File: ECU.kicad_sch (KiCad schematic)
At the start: 6 parts

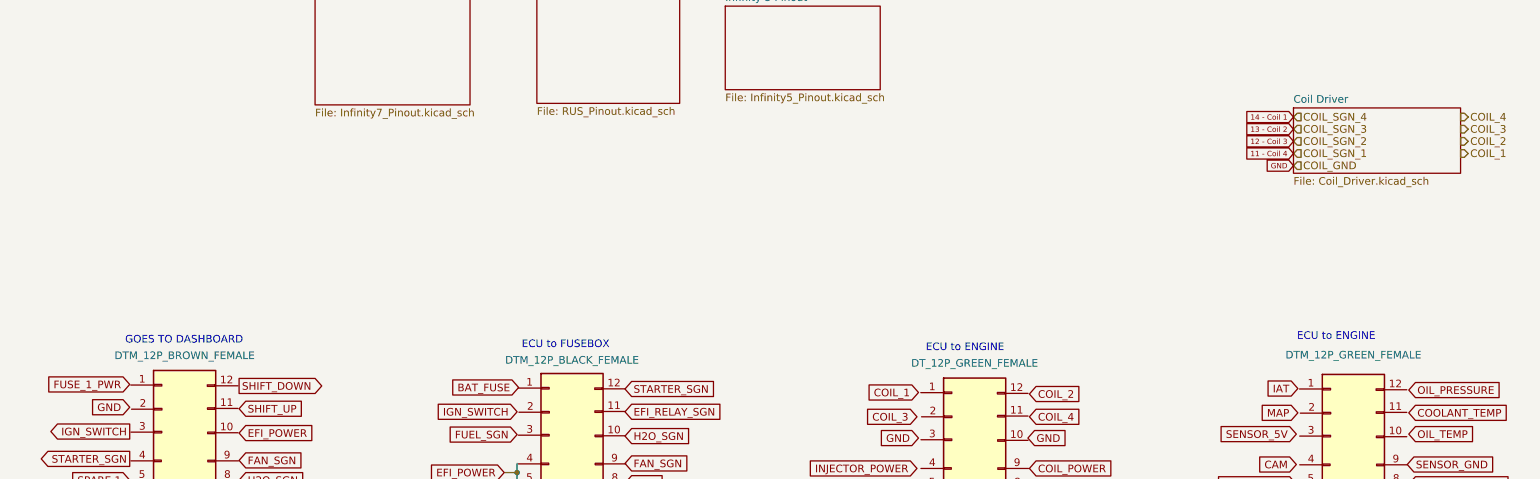
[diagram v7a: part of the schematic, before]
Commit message: Connector Numbers 1
Added Numbers to all of the connectors that were numbered and in KiCad so far
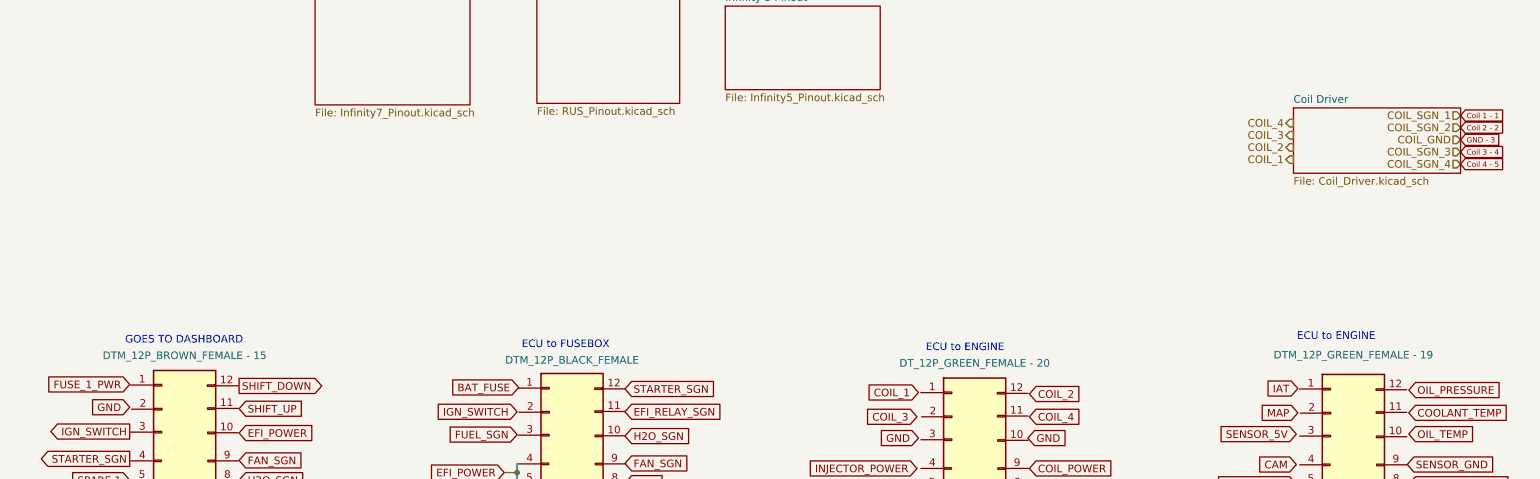
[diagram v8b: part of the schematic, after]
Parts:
- U?: value DTM_12P_BROWN_FEMALE -> DTM_12P_BROWN_FEMALE - 15
- U?: value DTM_12P_GREEN_FEMALE -> DTM_12P_GREEN_FEMALE - 19
- U?: value DT_12P_GREEN_FEMALE -> DT_12P_GREEN_FEMALE - 20
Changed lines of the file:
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@@
     )
   )
-  (global_label "GND" (shape input) (at 233.426 45.974 180) (fields_autoplaced)
-    (effects (font (size 0.889 0.889)) (justify right))
-    (property "Intersheet References" "${INTERSHEET_REFS}" (id 0) (at 229.0276 45.9185 0)
-      (effects (font (size 0.889 0.889)) (justify right) hide)
+  (global_label "GND - 3" (shape input) (at 261.366 41.656 0) (fields_autoplaced)
+    (effects (font (size 0.889 0.889)) (justify left))
+    (property "Intersheet References" "${INTERSHEET_REFS}" (id 0) (at 269.0664 41.6005 0)
+      (effects (font (size 0.889 0.889)) (justify left) hide)
     )
   )
@@
     )
   )
-  (global_label "11 - Coil 4" (shape input) (at 233.426 43.942 180) (fields_autoplaced)
-    (effects (font (size 0.889 0.889)) (justify right))
-    (property "Intersheet References" "${INTERSHEET_REFS}" (id 0) (at 223.4819 43.8865 0)
-      (effects (font (size 0.889 0.889)) (justify right) hide)
+  (global_label "Coil 4 - 5" (shape input) (at 261.366 45.72 0) (fields_autoplaced)
+    (effects (font (size 0.889 0.889)) (justify left))
+    (property "Intersheet References" "${INTERSHEET_REFS}" (id 0) (at 270.4634 45.6645 0)
+      (effects (font (size 0.889 0.889)) (justify left) hide)
     )
   )
@@
     )
   )
-  (global_label "12 - Coil 3" (shape input) (at 233.426 41.91 180) (fields_autoplaced)
-    (effects (font (size 0.889 0.889)) (justify right))
-    (property "Intersheet References" "${INTERSHEET_REFS}" (id 0) (at 223.4819 41.8545 0)
-      (effects (font (size 0.889 0.889)) (justify right) hide)
+  (global_label "Coil 3 - 4" (shape input) (at 261.366 43.688 0) (fields_autoplaced)
+    (effects (font (size 0.889 0.889)) (justify left))
+    (property "Intersheet References" "${INTERSHEET_REFS}" (id 0) (at 270.4634 43.6325 0)
+      (effects (font (size 0.889 0.889)) (justify left) hide)
     )
   )
@@
     )
   )
-  (global_label "13 - Coil 2" (shape input) (at 233.426 39.878 180) (fields_autoplaced)
-    (effects (font (size 0.889 0.889)) (justify right))
-    (property "Intersheet References" "${INTERSHEET_REFS}" (id 0) (at 223.4819 39.8225 0)
-      (effects (font (size 0.889 0.889)) (justify right) hide)
+  (global_label "Coil 2 - 2" (shape input) (at 261.366 39.624 0) (fields_autoplaced)
+    (effects (font (size 0.889 0.889)) (justify left))
+    (property "Intersheet References" "${INTERSHEET_REFS}" (id 0) (at 270.4634 39.5685 0)
+      (effects (font (size 0.889 0.889)) (justify left) hide)
     )
   )
@@
     )
   )
-  (global_label "14 - Coil 1" (shape input) (at 233.426 37.846 180) (fields_autoplaced)
-    (effects (font (size 0.889 0.889)) (justify right))
-    (property "Intersheet References" "${INTERSHEET_REFS}" (id 0) (at 223.4819 37.7905 0)
-      (effects (font (size 0.889 0.889)) (justify right) hide)
+  (global_label "Coil 1 - 1 " (shape input) (at 261.366 37.592 0) (fields_autoplaced)
+    (effects (font (size 0.889 0.889)) (justify left))
+    (property "Intersheet References" "${INTERSHEET_REFS}" (id 0) (at 271.1408 37.5365 0)
+      (effects (font (size 0.889 0.889)) (justify left) hide)
     )
   )
@@
     )
   )
-  (hierarchical_label "COIL_SGN_4" (shape input) (at 233.426 37.846 0)
-    (effects (font (size 1.27 1.27)) (justify left))
-  )
-  (hierarchical_label "COIL_4" (shape output) (at 261.366 37.846 0)
-    (effects (font (size 1.27 1.27)) (justify left))
-  )
-  (hierarchical_label "COIL_GND" (shape input) (at 233.426 45.974 0)
-    (effects (font (size 1.27 1.27)) (justify left))
-  )
-  (hierarchical_label "COIL_SGN_3" (shape input) (at 233.426 39.878 0)
-    (effects (font (size 1.27 1.27)) (justify left))
-  )
-  (hierarchical_label "COIL_SGN_2" (shape input) (at 233.426 41.91 0)
-    (effects (font (size 1.27 1.27)) (justify left))
-  )
-  (hierarchical_label "COIL_2" (shape output) (at 261.366 41.91 0)
-    (effects (font (size 1.27 1.27)) (justify left))
-  )
-  (hierarchical_label "COIL_1" (shape output) (at 261.366 43.942 0)
-    (effects (font (size 1.27 1.27)) (justify left))
-  )
-  (hierarchical_label "COIL_3" (shape output) (at 261.366 39.878 0)
-    (effects (font (size 1.27 1.27)) (justify left))
-  )
-  (hierarchical_label "COIL_SGN_1" (shape input) (at 233.426 43.942 0)
-    (effects (font (size 1.27 1.27)) (justify left))
+  (hierarchical_label "COIL_SGN_4" (shape input) (at 261.366 45.72 180)
+    (effects (font (size 1.27 1.27)) (justify right))
+  )
+  (hierarchical_label "COIL_4" (shape output) (at 233.426 38.862 180)
+    (effects (font (size 1.27 1.27)) (justify right))
+  )
+  (hierarchical_label "COIL_GND" (shape input) (at 261.366 41.656 180)
+    (effects (font (size 1.27 1.27)) (justify right))
+  )
+  (hierarchical_label "COIL_SGN_3" (shape input) (at 261.366 43.688 180)
+    (effects (font (size 1.27 1.27)) (justify right))
+  )
+  (hierarchical_label "COIL_SGN_2" (shape input) (at 261.366 39.624 180)
+    (effects (font (size 1.27 1.27)) (justify right))
+  )
+  (hierarchical_label "COIL_2" (shape output) (at 233.426 42.926 180)
+    (effects (font (size 1.27 1.27)) (justify right))
+  )
+  (hierarchical_label "COIL_1" (shape output) (at 233.426 44.958 180)
+    (effects (font (size 1.27 1.27)) (justify right))
+  )
+  (hierarchical_label "COIL_3" (shape output) (at 233.426 40.894 180)
+    (effects (font (size 1.27 1.27)) (justify right))
+  )
+  (hierarchical_label "COIL_SGN_1" (shape input) (at 261.366 37.592 180)
+    (effects (font (size 1.27 1.27)) (justify right))
   )
   (symbol (lib_id "Ty lib:ECU") (at 49.022 166.37 0) (unit 1)
@@
       (effects (font (size 1.27 1.27)) hide)
     )
-    (property "Value" "DTM_12P_BROWN_FEMALE" (id 1) (at 48.0441 77.724 0))
+    (property "Value" "DTM_12P_BROWN_FEMALE - 15" (id 1) (at 48.0441 77.724 0))
     (property "Footprint" "" (id 2) (at 47.752 103.124 0)
       (effects (font (size 1.27 1.27)) hide)
@@
       (effects (font (size 1.27 1.27)) hide)
     )
-    (property "Value" "DTM_12P_GREEN_FEMALE" (id 1) (at 243.4463 77.6224 0))
+    (property "Value" "DTM_12P_GREEN_FEMALE - 19" (id 1) (at 243.4463 77.6224 0))
     (property "Footprint" "" (id 2) (at 243.1542 103.7844 0)
       (effects (font (size 1.27 1.27)) hide)
@@
       (effects (font (size 1.27 1.27)) hide)
     )
-    (property "Value" "DT_12P_GREEN_FEMALE" (id 1) (at 180.1241 78.994 0))
+    (property "Value" "DT_12P_GREEN_FEMALE - 20" (id 1) (at 180.1241 78.994 0))
     (property "Footprint" "" (id 2) (at 179.832 104.394 0)
       (effects (font (size 1.27 1.27)) hide)
